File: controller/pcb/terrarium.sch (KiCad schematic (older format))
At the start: 55 parts, among them Q1 S8050, Q2 S8050, Q3 S8050, SW1 SW_Push, SW2 SW_Push, U1 ESP32-WROOM-32, U2 DS3231M, U3 LM1117-3.3

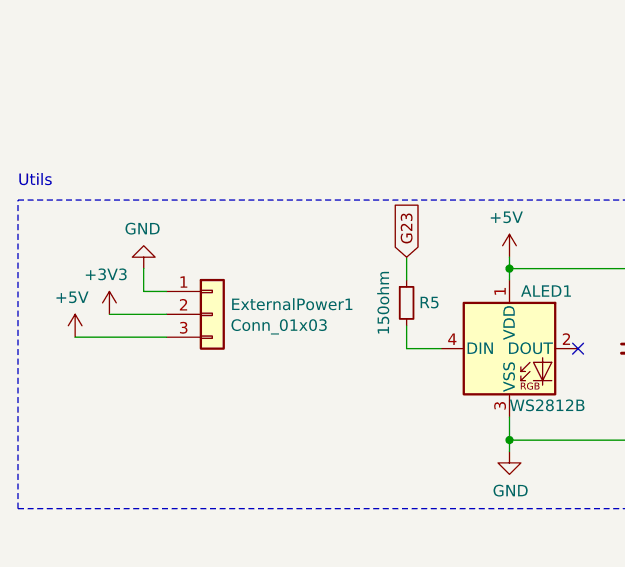
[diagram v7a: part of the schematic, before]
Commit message: wip: move to smd
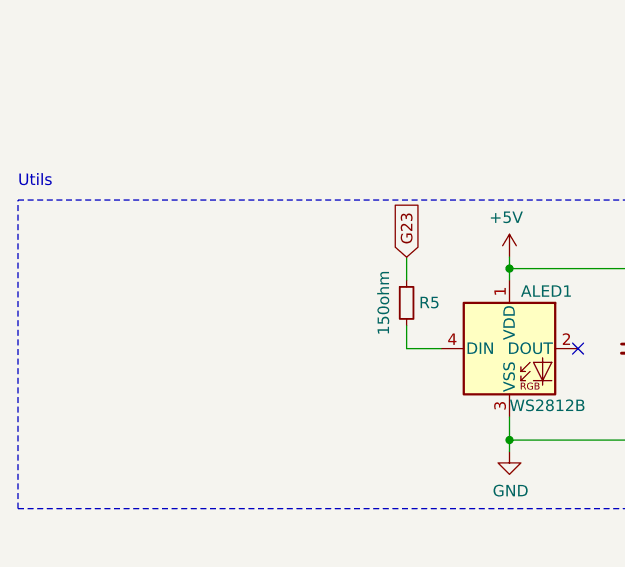
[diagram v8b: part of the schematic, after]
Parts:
- removed ExternalPower1: Conn_01x03, Connector_PinHeader_2.54mm:PinHeader_1x03_P2.54mm_Vertical, symbol Connector_Generic:Conn_01x03
- C1, C2, C3: footprint Capacitor_THT:C_Disc_D5.0mm_W2.5mm_P5.00mm -> Capacitor_SMD:C_1206_3216Metric
- LED1, LED2, LED3, LED4: footprint LED_THT:LED_D3.0mm_Clear -> LED_SMD:LED_1206_3216Metric
- R1, R10, R11, R12, R2, R3, R4, R5, R6, R7, R8, R9: footprint Resistor_THT:R_Axial_DIN0207_L6.3mm_D2.5mm_P7.62mm_Horizontal -> Resistor_SMD:R_1206_3216Metric
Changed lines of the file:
@@
 NoConn ~ 4950 1650
 NoConn ~ 3550 2800
-$Comp
-L Connector_Generic:Conn_01x03 ExternalPower1
-U 1 1 618715FE
-P 1550 6250
-F 0 "ExternalPower1" H 1630 6292 50  0000 L CNN
-F 1 "Conn_01x03" H 1630 6201 50  0000 L CNN
-F 2 "Connector_PinHeader_2.54mm:PinHeader_1x03_P2.54mm_Vertical" H 1550 6250 50  0001 C CNN
-F 3 "~" H 1550 6250 50  0001 C CNN
-	1    1550 6250
-	1    0    0    -1
-$EndComp
 Text GLabel 2000 1100 0    50   Input ~ 0
 SCL
@@
 	1050 1800 1150 1800
 $Comp
-L power:GND #PWR0103
-U 1 1 618F640C
-P 1250 6050
-F 0 "#PWR0103" H 1250 5800 50  0001 C CNN
-F 1 "GND" H 1255 5877 50  0000 C CNN
-F 2 "" H 1250 6050 50  0001 C CNN
-F 3 "" H 1250 6050 50  0001 C CNN
-	1    1250 6050
-	-1   0    0    1
-$EndComp
-Wire Wire Line
-	1250 6050 1250 6150
-Wire Wire Line
-	1250 6150 1350 6150
-$Comp
 L power:GND #PWR0104
 U 1 1 618FA125
@@
 	900  1900 1150 1900
 $Comp
-L power:+5V #PWR0123
-U 1 1 619AC140
-P 950 6350
-F 0 "#PWR0123" H 950 6200 50  0001 C CNN
-F 1 "+5V" H 965 6523 50  0000 C CNN
-F 2 "" H 950 6350 50  0001 C CNN
-F 3 "" H 950 6350 50  0001 C CNN
-	1    950  6350
-	-1   0    0    -1
-$EndComp
-$Comp
-L power:+3V3 #PWR0126
-U 1 1 619C436C
-P 1100 6250
-F 0 "#PWR0126" H 1100 6100 50  0001 C CNN
-F 1 "+3V3" H 1115 6423 50  0000 C CNN
-F 2 "" H 1100 6250 50  0001 C CNN
-F 3 "" H 1100 6250 50  0001 C CNN
-	1    1100 6250
-	-1   0    0    -1
-$EndComp
-$Comp
 L power:+3V3 #PWR0127
 U 1 1 619C4CA5
@@
 Wire Wire Line
 	1750 1900 2000 1900
-Wire Wire Line
-	1100 6250 1350 6250
-Wire Wire Line
-	950  6350 1350 6350
 Text GLabel 4750 2500 0    50   Input ~ 0
 G26
@@
 F 0 "R1" V 6650 1900 50  0000 C CNN
 F 1 "150ohm" V 6450 1900 50  0000 C CNN
-F 2 "Resistor_THT:R_Axial_DIN0207_L6.3mm_D2.5mm_P7.62mm_Horizontal" H 6550 1900 50  0001 C CNN
+F 2 "Resistor_SMD:R_1206_3216Metric" H 6550 1900 50  0001 C CNN
 F 3 "~" H 6550 1900 50  0001 C CNN
 	1    6550 1900
@@
 F 0 "LED1" H 6300 1800 50  0000 R CNN
 F 1 "ACTIVE" H 6300 2000 50  0000 R CNN
-F 2 "LED_THT:LED_D3.0mm_Clear" H 6200 1900 50  0001 C CNN
+F 2 "LED_SMD:LED_1206_3216Metric" H 6200 1900 50  0001 C CNN
 F 3 "~" H 6200 1900 50  0001 C CNN
 	1    6200 1900
@@
 F 0 "R3" V 6700 3500 50  0000 C CNN
 F 1 "150ohm" V 6500 3500 50  0000 C CNN
-F 2 "Resistor_THT:R_Axial_DIN0207_L6.3mm_D2.5mm_P7.62mm_Horizontal" H 6600 3500 50  0001 C CNN
+F 2 "Resistor_SMD:R_1206_3216Metric" H 6600 3500 50  0001 C CNN
 F 3 "~" H 6600 3500 50  0001 C CNN
 	1    6600 3500
@@
 F 0 "LED2" H 6350 3400 50  0000 R CNN
 F 1 "ACTIVE" H 6350 3600 50  0000 R CNN
-F 2 "LED_THT:LED_D3.0mm_Clear" H 6250 3500 50  0001 C CNN
+F 2 "LED_SMD:LED_1206_3216Metric" H 6250 3500 50  0001 C CNN
 F 3 "~" H 6250 3500 50  0001 C CNN
 	1    6250 3500
@@
 F 0 "R4" V 7350 3600 50  0000 C CNN
 F 1 "R_Small" V 7150 3600 50  0000 C CNN
-F 2 "Resistor_THT:R_Axial_DIN0207_L6.3mm_D2.5mm_P7.62mm_Horizontal" H 7250 3600 50  0001 C CNN
+F 2 "Resistor_SMD:R_1206_3216Metric" H 7250 3600 50  0001 C CNN
 F 3 "~" H 7250 3600 50  0001 C CNN
 	1    7250 3600
@@
 F 0 "R2" V 7300 2000 50  0000 C CNN
 F 1 "R_Small" V 7100 2000 50  0000 C CNN
-F 2 "Resistor_THT:R_Axial_DIN0207_L6.3mm_D2.5mm_P7.62mm_Horizontal" H 7200 2000 50  0001 C CNN
+F 2 "Resistor_SMD:R_1206_3216Metric" H 7200 2000 50  0001 C CNN
 F 3 "~" H 7200 2000 50  0001 C CNN
 	1    7200 2000
@@
 F 0 "C1" H 3492 6446 50  0000 L CNN
 F 1 "10pF" H 3492 6355 50  0000 L CNN
-F 2 "Capacitor_THT:C_Disc_D5.0mm_W2.5mm_P5.00mm" H 3400 6400 50  0001 C CNN
+F 2 "Capacitor_SMD:C_1206_3216Metric" H 3400 6400 50  0001 C CNN
 F 3 "~" H 3400 6400 50  0001 C CNN
 	1    3400 6400
@@
 F 0 "R5" H 2500 6200 50  0000 C CNN
 F 1 "150ohm" V 2300 6200 50  0000 C CNN
-F 2 "Resistor_THT:R_Axial_DIN0207_L6.3mm_D2.5mm_P7.62mm_Horizontal" H 2400 6200 50  0001 C CNN
+F 2 "Resistor_SMD:R_1206_3216Metric" H 2400 6200 50  0001 C CNN
 F 3 "~" H 2400 6200 50  0001 C CNN
 	1    2400 6200
@@
 F 0 "R7" V 6700 5050 50  0000 C CNN
 F 1 "150ohm" V 6500 5050 50  0000 C CNN
-F 2 "Resistor_THT:R_Axial_DIN0207_L6.3mm_D2.5mm_P7.62mm_Horizontal" H 6600 5050 50  0001 C CNN
+F 2 "Resistor_SMD:R_1206_3216Metric" H 6600 5050 50  0001 C CNN
 F 3 "~" H 6600 5050 50  0001 C CNN
 	1    6600 5050
@@
 F 0 "LED3" H 6350 4950 50  0000 R CNN
 F 1 "ACTIVE" H 6350 5150 50  0000 R CNN
-F 2 "LED_THT:LED_D3.0mm_Clear" H 6250 5050 50  0001 C CNN
+F 2 "LED_SMD:LED_1206_3216Metric" H 6250 5050 50  0001 C CNN
 F 3 "~" H 6250 5050 50  0001 C CNN
 	1    6250 5050
@@
 F 0 "R6" V 7350 5150 50  0000 C CNN
 F 1 "R_Small" V 7150 5150 50  0000 C CNN
-F 2 "Resistor_THT:R_Axial_DIN0207_L6.3mm_D2.5mm_P7.62mm_Horizontal" H 7250 5150 50  0001 C CNN
+F 2 "Resistor_SMD:R_1206_3216Metric" H 7250 5150 50  0001 C CNN
 F 3 "~" H 7250 5150 50  0001 C CNN
 	1    7250 5150
@@
 F 0 "R9" H 1750 8000 50  0000 C CNN
 F 1 "4.7k" V 1550 8000 50  0000 C CNN
-F 2 "Resistor_THT:R_Axial_DIN0207_L6.3mm_D2.5mm_P7.62mm_Horizontal" H 1650 8000 50  0001 C CNN
+F 2 "Resistor_SMD:R_1206_3216Metric" H 1650 8000 50  0001 C CNN
 F 3 "~" H 1650 8000 50  0001 C CNN
 	1    1650 8000
@@
 F 0 "R8" V 1700 8550 50  0000 C CNN
 F 1 "4.7k" V 1500 8550 50  0000 C CNN
-F 2 "Resistor_THT:R_Axial_DIN0207_L6.3mm_D2.5mm_P7.62mm_Horizontal" H 1600 8550 50  0001 C CNN
+F 2 "Resistor_SMD:R_1206_3216Metric" H 1600 8550 50  0001 C CNN
 F 3 "~" H 1600 8550 50  0001 C CNN
 	1    1600 8550
@@
 F 0 "R11" V 12550 1350 50  0000 C CNN
 F 1 "10k" V 12350 1350 50  0000 C CNN
-F 2 "Resistor_THT:R_Axial_DIN0207_L6.3mm_D2.5mm_P7.62mm_Horizontal" H 12450 1350 50  0001 C CNN
+F 2 "Resistor_SMD:R_1206_3216Metric" H 12450 1350 50  0001 C CNN
 F 3 "~" H 12450 1350 50  0001 C CNN
 	1    12450 1350
@@
 F 0 "R10" V 14500 1350 50  0000 C CNN
 F 1 "10k" V 14300 1350 50  0000 C CNN
-F 2 "Resistor_THT:R_Axial_DIN0207_L6.3mm_D2.5mm_P7.62mm_Horizontal" H 14400 1350 50  0001 C CNN
+F 2 "Resistor_SMD:R_1206_3216Metric" H 14400 1350 50  0001 C CNN
 F 3 "~" H 14400 1350 50  0001 C CNN
 	1    14400 1350
@@
 F 0 "C2" H 13092 5696 50  0000 L CNN
 F 1 "10uF" H 13092 5605 50  0000 L CNN
-F 2 "Capacitor_THT:C_Disc_D5.0mm_W2.5mm_P5.00mm" H 13000 5650 50  0001 C CNN
+F 2 "Capacitor_SMD:C_1206_3216Metric" H 13000 5650 50  0001 C CNN
 F 3 "~" H 13000 5650 50  0001 C CNN
 	1    13000 5650
@@
 F 0 "C3" H 14092 5696 50  0000 L CNN
 F 1 "47uF" H 14092 5605 50  0000 L CNN
-F 2 "Capacitor_THT:C_Disc_D5.0mm_W2.5mm_P5.00mm" H 14000 5650 50  0001 C CNN
+F 2 "Capacitor_SMD:C_1206_3216Metric" H 14000 5650 50  0001 C CNN
 F 3 "~" H 14000 5650 50  0001 C CNN
 	1    14000 5650
@@
 F 0 "R12" V 14400 6100 50  0000 C CNN
 F 1 "300" V 14200 6100 50  0000 C CNN
-F 2 "Resistor_THT:R_Axial_DIN0207_L6.3mm_D2.5mm_P7.62mm_Horizontal" H 14300 6100 50  0001 C CNN
+F 2 "Resistor_SMD:R_1206_3216Metric" H 14300 6100 50  0001 C CNN
 F 3 "~" H 14300 6100 50  0001 C CNN
 	1    14300 6100
@@
 F 0 "LED4" H 14800 5600 50  0000 R CNN
 F 1 "POWER" H 14800 5800 50  0000 R CNN
-F 2 "LED_THT:LED_D3.0mm_Clear" H 14700 5700 50  0001 C CNN
+F 2 "LED_SMD:LED_1206_3216Metric" H 14700 5700 50  0001 C CNN
 F 3 "~" H 14700 5700 50  0001 C CNN
 	1    14700 5700
